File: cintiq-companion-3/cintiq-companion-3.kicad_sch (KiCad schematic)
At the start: 4 parts, among them J1 13HD_eDP, J2 13HD_penpanel, J3 13HD_buttonboard, J4 13HD_fingerpanel

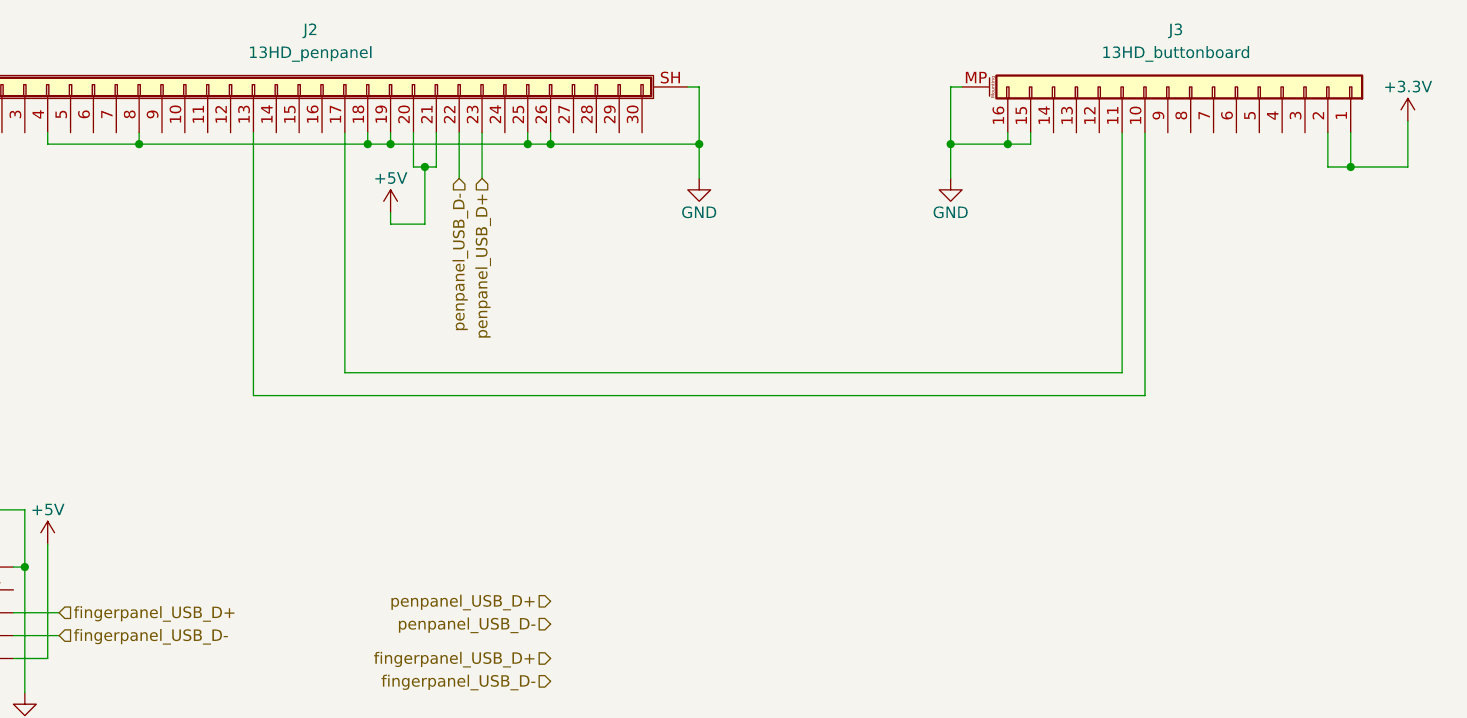
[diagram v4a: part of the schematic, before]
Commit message: Wired up all buttons
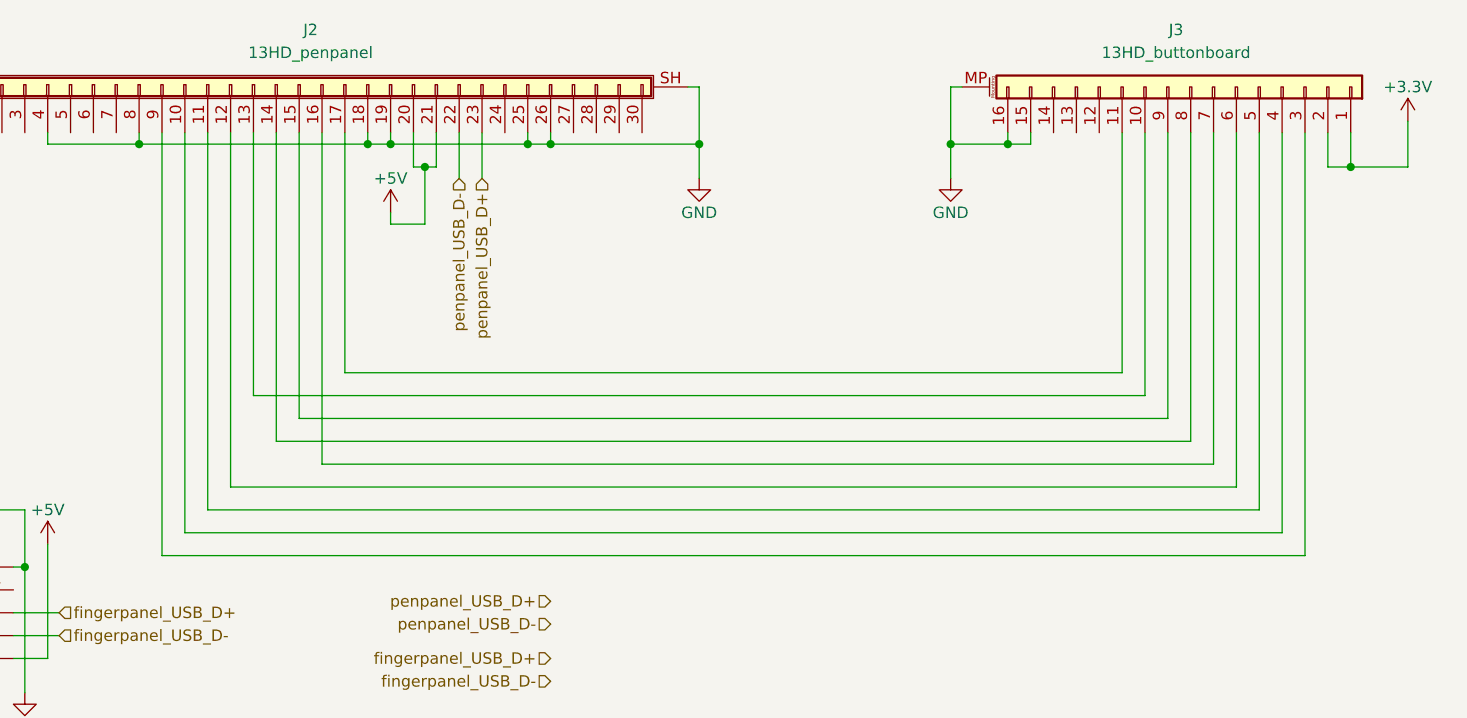
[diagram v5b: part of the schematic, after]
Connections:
- net at J2.10 (Pin_10): now also J3.4 (Pin_4)
- net at J2.11 (Pin_11): now also J3.5 (Pin_5)
- net at J2.12 (Pin_12): now also J3.6 (Pin_6)
- net at J2.14 (Pin_14): now also J3.8 (Pin_8)
- net at J2.15 (Pin_15): now also J3.9 (Pin_9)
- net at J2.16 (Pin_16): now also J3.7 (Pin_7)
- net at J2.9 (Pin_9): now also J3.3 (Pin_3)
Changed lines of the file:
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@@
+	(wire
+		(pts
+			(xy 63.5 78.74) (xy 63.5 31.75)
+		)
+		(stroke
+			(width 0)
+			(type default)
+		)
+	)
 	(wire
 		(pts
@@
 	(wire
 		(pts
+			(xy 76.2 66.04) (xy 76.2 31.75)
+		)
+		(stroke
+			(width 0)
+			(type default)
+		)
+	)
+	(wire
+		(pts
 			(xy 50.8 90.17) (xy 46.99 90.17)
 		)
@@
 	(wire
 		(pts
+			(xy 180.34 68.58) (xy 81.28 68.58)
+		)
+		(stroke
+			(width 0)
+			(type default)
+		)
+	)
+	(wire
+		(pts
+			(xy 187.96 76.2) (xy 66.04 76.2)
+		)
+		(stroke
+			(width 0)
+			(type default)
+		)
+	)
+	(wire
+		(pts
 			(xy 170.18 31.75) (xy 170.18 58.42)
 		)
@@
 	(wire
 		(pts
+			(xy 68.58 73.66) (xy 68.58 31.75)
+		)
+		(stroke
+			(width 0)
+			(type default)
+		)
+	)
+	(wire
+		(pts
+			(xy 185.42 31.75) (xy 185.42 73.66)
+		)
+		(stroke
+			(width 0)
+			(type default)
+		)
+	)
+	(wire
+		(pts
+			(xy 81.28 68.58) (xy 81.28 31.75)
+		)
+		(stroke
+			(width 0)
+			(type default)
+		)
+	)
+	(wire
+		(pts
 			(xy 250.19 64.77) (xy 248.92 64.77)
 		)
@@
 	(wire
 		(pts
+			(xy 185.42 73.66) (xy 68.58 73.66)
+		)
+		(stroke
+			(width 0)
+			(type default)
+		)
+	)
+	(wire
+		(pts
 			(xy 248.92 39.37) (xy 248.92 46.99)
 		)
@@
 	(wire
 		(pts
+			(xy 66.04 76.2) (xy 66.04 31.75)
+		)
+		(stroke
+			(width 0)
+			(type default)
+		)
+	)
+	(wire
+		(pts
 			(xy 86.36 31.75) (xy 86.36 33.02)
 		)
@@
 	(wire
 		(pts
+			(xy 190.5 78.74) (xy 63.5 78.74)
+		)
+		(stroke
+			(width 0)
+			(type default)
+		)
+	)
+	(wire
+		(pts
+			(xy 71.12 71.12) (xy 71.12 31.75)
+		)
+		(stroke
+			(width 0)
+			(type default)
+		)
+	)
+	(wire
+		(pts
 			(xy 93.98 31.75) (xy 93.98 35.56)
 		)
@@
 	(wire
 		(pts
+			(xy 187.96 31.75) (xy 187.96 76.2)
+		)
+		(stroke
+			(width 0)
+			(type default)
+		)
+	)
+	(wire
+		(pts
 			(xy 246.38 59.69) (xy 250.19 59.69)
 		)
@@
 	(wire
 		(pts
+			(xy 190.5 31.75) (xy 190.5 78.74)
+		)
+		(stroke
+			(width 0)
+			(type default)
+		)
+	)
+	(wire
+		(pts
+			(xy 182.88 31.75) (xy 182.88 71.12)
+		)
+		(stroke
+			(width 0)
+			(type default)
+		)
+	)
+	(wire
+		(pts
 			(xy 73.66 31.75) (xy 73.66 60.96)
 		)
@@
 	(wire
 		(pts
+			(xy 177.8 31.75) (xy 177.8 66.04)
+		)
+		(stroke
+			(width 0)
+			(type default)
+		)
+	)
+	(wire
+		(pts
 			(xy 92.71 41.91) (xy 92.71 35.56)
 		)
@@
 	(wire
 		(pts
+			(xy 175.26 63.5) (xy 78.74 63.5)
+		)
+		(stroke
+			(width 0)
+			(type default)
+		)
+	)
+	(wire
+		(pts
 			(xy 170.18 58.42) (xy 83.82 58.42)
 		)
@@
 	(wire
 		(pts
+			(xy 180.34 31.75) (xy 180.34 68.58)
+		)
+		(stroke
+			(width 0)
+			(type default)
+		)
+	)
+	(wire
+		(pts
+			(xy 175.26 31.75) (xy 175.26 63.5)
+		)
+		(stroke
+			(width 0)
+			(type default)
+		)
+	)
+	(wire
+		(pts
 			(xy 50.8 31.75) (xy 50.8 33.02)
 		)
@@
 	(wire
 		(pts
+			(xy 78.74 63.5) (xy 78.74 31.75)
+		)
+		(stroke
+			(width 0)
+			(type default)
+		)
+	)
+	(wire
+		(pts
 			(xy 193.04 35.56) (xy 193.04 31.75)
 		)
@@
 	(wire
 		(pts
+			(xy 182.88 71.12) (xy 71.12 71.12)
+		)
+		(stroke
+			(width 0)
+			(type default)
+		)
+	)
+	(wire
+		(pts
 			(xy 151.13 33.02) (xy 151.13 26.67)
 		)
@@
 		)
 		(stroke
+			(width 0)
+			(type default)
+		)
+	)
+	(wire
+		(pts
+			(xy 177.8 66.04) (xy 76.2 66.04)
+		)
+		(stroke

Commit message: Completed pinout + added full board pics
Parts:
- added R1, R2: 4.7kΩ, symbol Device:R_Small
- added R3: 47kΩ, symbol Device:R_Small
- added TP1: Something, symbol Connector:TestPoint
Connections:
- net GND: now also R1.2, R2.2, R3.2
- net middletopbutton: now reaches J2.10 (Pin_10), J3.4 (Pin_4)
- net middlebottombutton: now reaches J2.11 (Pin_11), J3.5 (Pin_5)
- net bottombutton: now reaches J2.12 (Pin_12), J3.6 (Pin_6)
- net rightbutton: now reaches J2.13 (Pin_13), J3.10 (Pin_10)
- net upbutton: now reaches J2.14 (Pin_14), J3.8 (Pin_8)
- net leftbutton: now reaches J2.15 (Pin_15), J3.9 (Pin_9)
- net downbutton: now reaches J2.16 (Pin_16), J3.7 (Pin_7)
- net middlebutton: now reaches J2.17 (Pin_17), J3.11 (Pin_11)
- net RTD2483AD_pin_105: now reaches J2.3 (Pin_3)
- net RTD2483AD_pin_105: now also R1.1
- net NC_i2c??: now reaches J2.5 (Pin_5)
- net NC_i2c?: now reaches J2.6 (Pin_6)
- net RTD2483AD_pin_110: now reaches J2.7 (Pin_7)
- net RTD2483AD_pin_110: now also R2.1
- net topbutton: now reaches J2.9 (Pin_9), J3.3 (Pin_3)
- net at J1.1 (Pin_1): now also TP1.1
- net eDP_AUX-+: now reaches J1.10 (Pin_10)
- net eDP_HPD: now reaches J1.16 (Pin_16)
- net eDP_HPD: now also R3.1
- net BL_return_????: now reaches J1.21 (Pin_21)
- net BL_return_???: now reaches J1.22 (Pin_22)
- net BL_return_??: now reaches J1.23 (Pin_23)
- net BL_return_?: now reaches J1.24 (Pin_24)
- net eDP_L??+-: now reaches J1.3 (Pin_3)
- net eDP_L??-+: now reaches J1.4 (Pin_4)
- net eDP_L?+-: now reaches J1.6 (Pin_6)
- net eDP_L?-+: now reaches J1.7 (Pin_7)
- net eDP_AUX+-: now reaches J1.9 (Pin_9)
- no-connect marks 0 -> 20

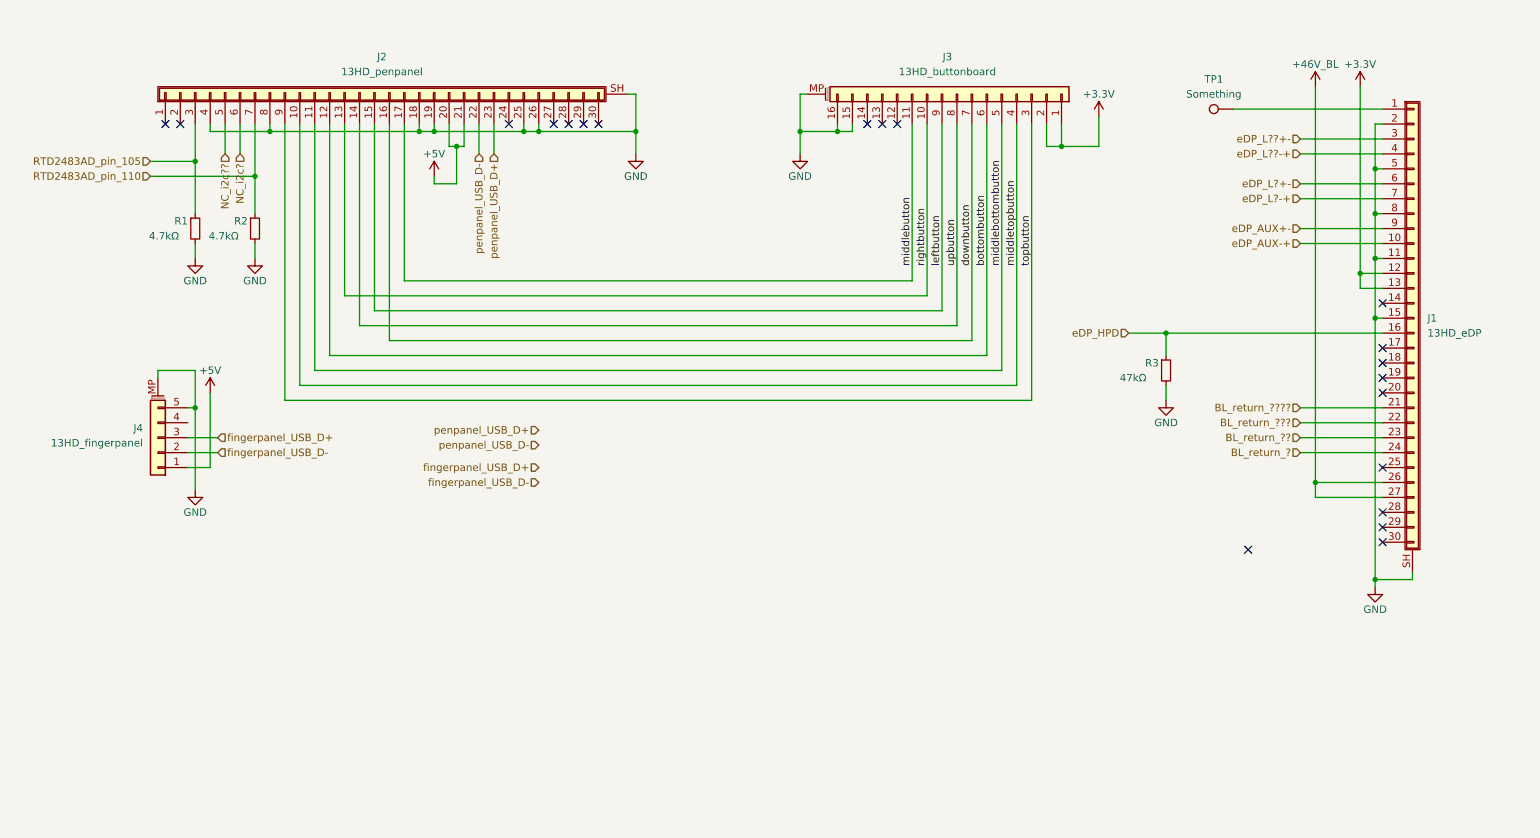
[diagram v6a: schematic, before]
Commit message: Added eDP pinout/polarity
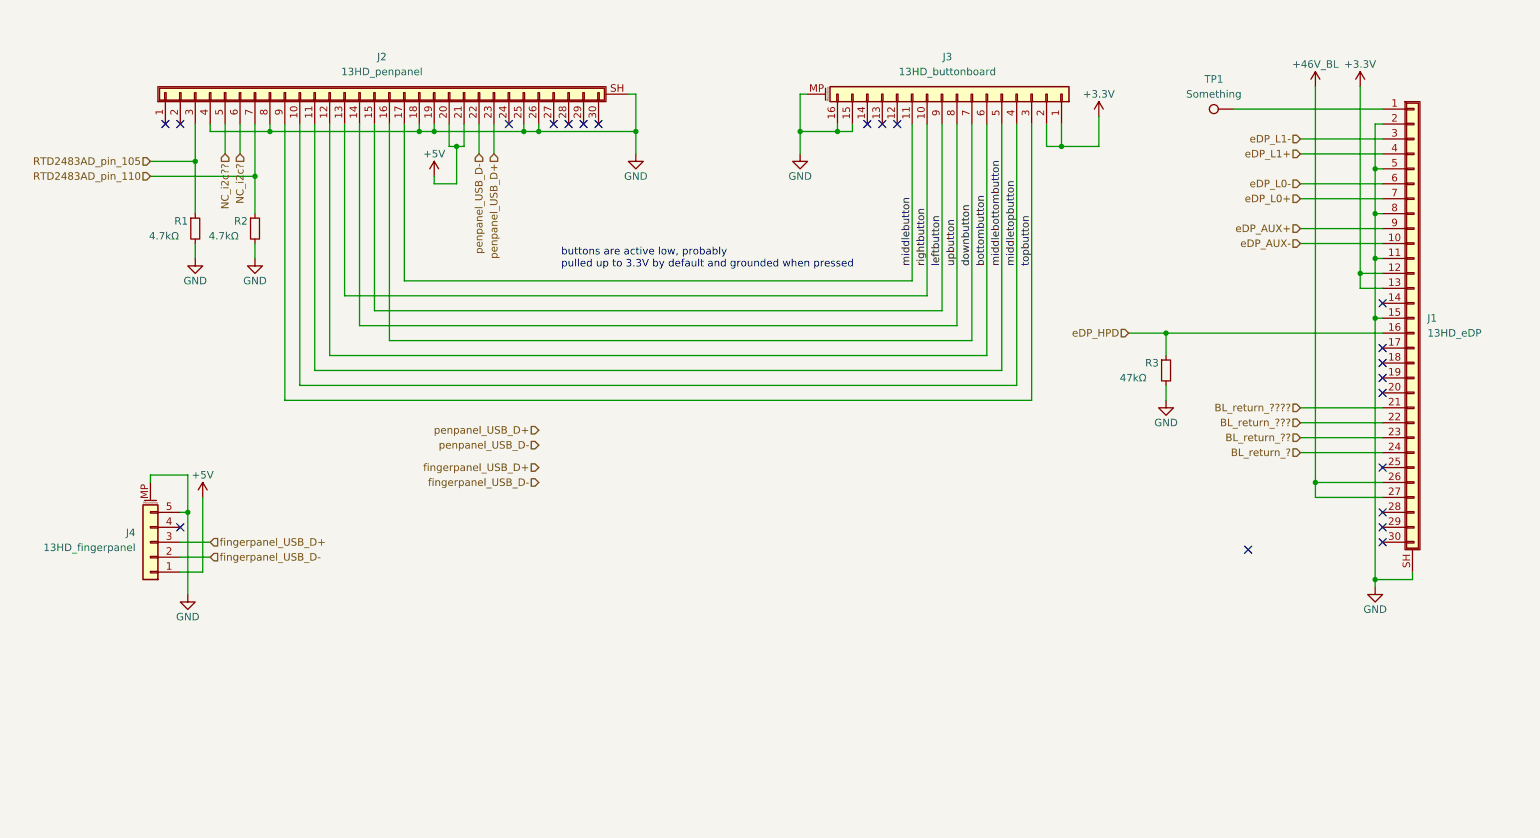
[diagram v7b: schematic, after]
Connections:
- net eDP_AUX+- renamed eDP_AUX+
- net eDP_AUX-+ renamed eDP_AUX-
- net eDP_L?+- renamed eDP_L0-
- net eDP_L?-+ renamed eDP_L0+
- net eDP_L??+- renamed eDP_L1-
- net eDP_L??-+ renamed eDP_L1+
- no-connect marks 20 -> 21
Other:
- note added: "buttons are active low, probably pulled up to 3.3V by default and grounded when pressed"
- moved on the sheet: J4
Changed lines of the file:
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@@
 	)
 	(junction
-		(at 48.26 80.01)
+		(at 46.99 97.79)
 		(diameter 0)
 		(color 0 0 0 0)
@@
 	)
 	(no_connect
+		(at 45.72 100.33)
+	)
+	(no_connect
 		(at 227.33 104.14)
 	)
@@
 	(wire
 		(pts
-			(xy 50.8 90.17) (xy 46.99 90.17)
+			(xy 49.53 107.95) (xy 45.72 107.95)
 		)
 		(stroke
@@
 	(wire
 		(pts
-			(xy 48.26 73.66) (xy 48.26 80.01)
+			(xy 46.99 91.44) (xy 46.99 97.79)
 		)
 		(stroke
@@
 	(wire
 		(pts
-			(xy 52.07 85.09) (xy 46.99 85.09)
+			(xy 50.8 102.87) (xy 45.72 102.87)
 		)
 		(stroke
@@
 	(wire
 		(pts
-			(xy 48.26 73.66) (xy 41.91 73.66)
+			(xy 46.99 91.44) (xy 40.64 91.44)
 		)
 		(stroke
@@
 	(wire
 		(pts
-			(xy 48.26 80.01) (xy 46.99 80.01)
+			(xy 46.99 97.79) (xy 45.72 97.79)
 		)
 		(stroke
@@
 	(wire
 		(pts
-			(xy 41.91 74.93) (xy 41.91 73.66)
+			(xy 40.64 92.71) (xy 40.64 91.44)
 		)
 		(stroke
@@
 	(wire
 		(pts
-			(xy 48.26 93.98) (xy 48.26 80.01)
+			(xy 46.99 111.76) (xy 46.99 97.79)
 		)
 		(stroke
@@
 	(wire
 		(pts
-			(xy 52.07 87.63) (xy 46.99 87.63)
+			(xy 50.8 105.41) (xy 45.72 105.41)
 		)
 		(stroke
@@
 	(wire
 		(pts
-			(xy 50.8 77.47) (xy 50.8 90.17)
+			(xy 49.53 95.25) (xy 49.53 107.95)
 		)
 		(stroke
@@
 			(width 0)
 			(type default)
+		)
+	)
+	(text "buttons are active low, probably\npulled up to 3.3V by default and grounded when pressed"
+		(exclude_from_sim no)
+		(at 110.49 54.61 0)
+		(effects
+			(font
+				(size 1.27 1.27)
+			)
+			(justify left)
 		)
 	)
@@
 		)
 	)
-	(hierarchical_label "eDP_AUX-+"
+	(hierarchical_label "eDP_AUX-"
 		(shape input)
 		(at 236.22 52.07 180)
@@
 		)
 	)
-	(hierarchical_label "eDP_AUX+-"
+	(hierarchical_label "eDP_AUX+"
 		(shape input)
 		(at 236.22 49.53 180)
@@
 		)
 	)
-	(hierarchical_label "eDP_L??+-"
+	(hierarchical_label "eDP_L1-"
 		(shape input)
 		(at 236.22 34.29 180)
@@
 	(hierarchical_label "fingerpanel_USB_D-"
 		(shape input)
-		(at 52.07 87.63 0)
+		(at 50.8 105.41 0)
 		(fields_autoplaced yes)
 		(effects
@@
 		)
 	)
-	(hierarchical_label "eDP_L?+-"
+	(hierarchical_label "eDP_L0-"
 		(shape input)
 		(at 236.22 41.91 180)
@@
 		)
 	)
-	(hierarchical_label "eDP_L??-+"
+	(hierarchical_label "eDP_L1+"
 		(shape input)
 		(at 236.22 36.83 180)
@@
 		)
 	)
-	(hierarchical_label "eDP_L?-+"
+	(hierarchical_label "eDP_L0+"
 		(shape input)
 		(at 236.22 44.45 180)
@@
 	(hierarchical_label "fingerpanel_USB_D+"
 		(shape input)
-		(at 52.07 85.09 0)
+		(at 50.8 102.87 0)
 		(fields_autoplaced yes)
 		(effects
@@
 	(symbol
 		(lib_id "power:+5V")
-		(at 50.8 77.47 0)
+		(at 49.53 95.25 0)
 		(unit 1)
 		(exclude_from_sim no)
@@
 		(dnp no)
 		(property "Reference" "#PWR05"
-			(at 50.8 81.28 0)
+			(at 49.53 99.06 0)
 			(effects
 				(font
@@
 		)
 		(property "Value" "+5V"
-			(at 50.8 73.66 0)
+			(at 49.53 91.44 0)
 			(effects
 				(font
@@
 		)
 		(property "Footprint" ""
-			(at 50.8 77.47 0)
+			(at 49.53 95.25 0)
 			(effects
 				(font
@@
 		)
 		(property "Datasheet" ""
-			(at 50.8 77.47 0)
+			(at 49.53 95.25 0)
 			(effects
 				(font
@@
 		)
 		(property "Description" "Power symbol creates a global label with name \"+5V\""
-			(at 50.8 77.47 0)
+			(at 49.53 95.25 0)
 			(effects
 				(font
@@
 	(symbol
 		(lib_id "power:GND")
-		(at 48.26 93.98 0)
+		(at 46.99 111.76 0)
 		(unit 1)
 		(exclude_from_sim no)
@@
 		(dnp no)
 		(property "Reference" "#PWR01"
-			(at 48.26 100.33 0)
+			(at 46.99 118.11 0)
 			(effects
 				(font
@@
 		)
 		(property "Value" "GND"
-			(at 48.26 97.79 0)
+			(at 46.99 115.57 0)
 			(effects
 				(font
@@
 		)
 		(property "Footprint" ""
-			(at 48.26 93.98 0)
+			(at 46.99 111.76 0)
 			(effects
 				(font
@@
 		)
 		(property "Datasheet" ""
-			(at 48.26 93.98 0)
+			(at 46.99 111.76 0)
 			(effects
 				(font
@@
 		)
 		(property "Description" "Power symbol creates a global label with name \"GND\" , ground"
-			(at 48.26 93.98 0)
+			(at 46.99 111.76 0)
 			(effects
 				(font
@@
 	(symbol
 		(lib_id "Connector_Generic_MountingPin:Conn_01x05_MountingPin")
-		(at 41.91 85.09 180)
+		(at 40.64 102.87 180)
 		(unit 1)
 		(exclude_from_sim no)
@@
 		(fields_autoplaced yes)
 		(property "Reference" "J4"
-			(at 39.37 83.4643 0)
+			(at 38.1 101.2443 0)
 			(effects
 				(font
@@
 		)
 		(property "Value" "13HD_fingerpanel"
-			(at 39.37 86.0043 0)
+			(at 38.1 103.7843 0)
 			(effects
 				(font
@@
 		)
 		(property "Footprint" ""
-			(at 41.91 85.09 0)
+			(at 40.64 102.87 0)
 			(effects
 				(font
@@
 		)
 		(property "Datasheet" "~"
-			(at 41.91 85.09 0)
+			(at 40.64 102.87 0)
 			(effects
 				(font
@@
 		)
 		(property "Description" "Generic connectable mounting pin connector, single row, 01x05, script generated (kicad-library-utils/schlib/autogen/connector/)"
-			(at 41.91 85.09 0)
-			(effects
-				(font
+			(at 40.64 102.87 0)
+			(effects
+				(font
